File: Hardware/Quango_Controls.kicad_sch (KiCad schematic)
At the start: 36 parts, among them J1 Conn_01x12_Male, J10 Gate_Out, J2 Conn_01x16_Male, J3 Conn_01x14_Male, J4 Conn_01x12_Male, J5 CV_A, J6 CV_B, J7 Out, J8 USB_C_Receptacle, J9 Midi_In, SW1 SW_Push, SW2 SW_Push, SW3 Octave_Switch, U1 STF202-22T1G

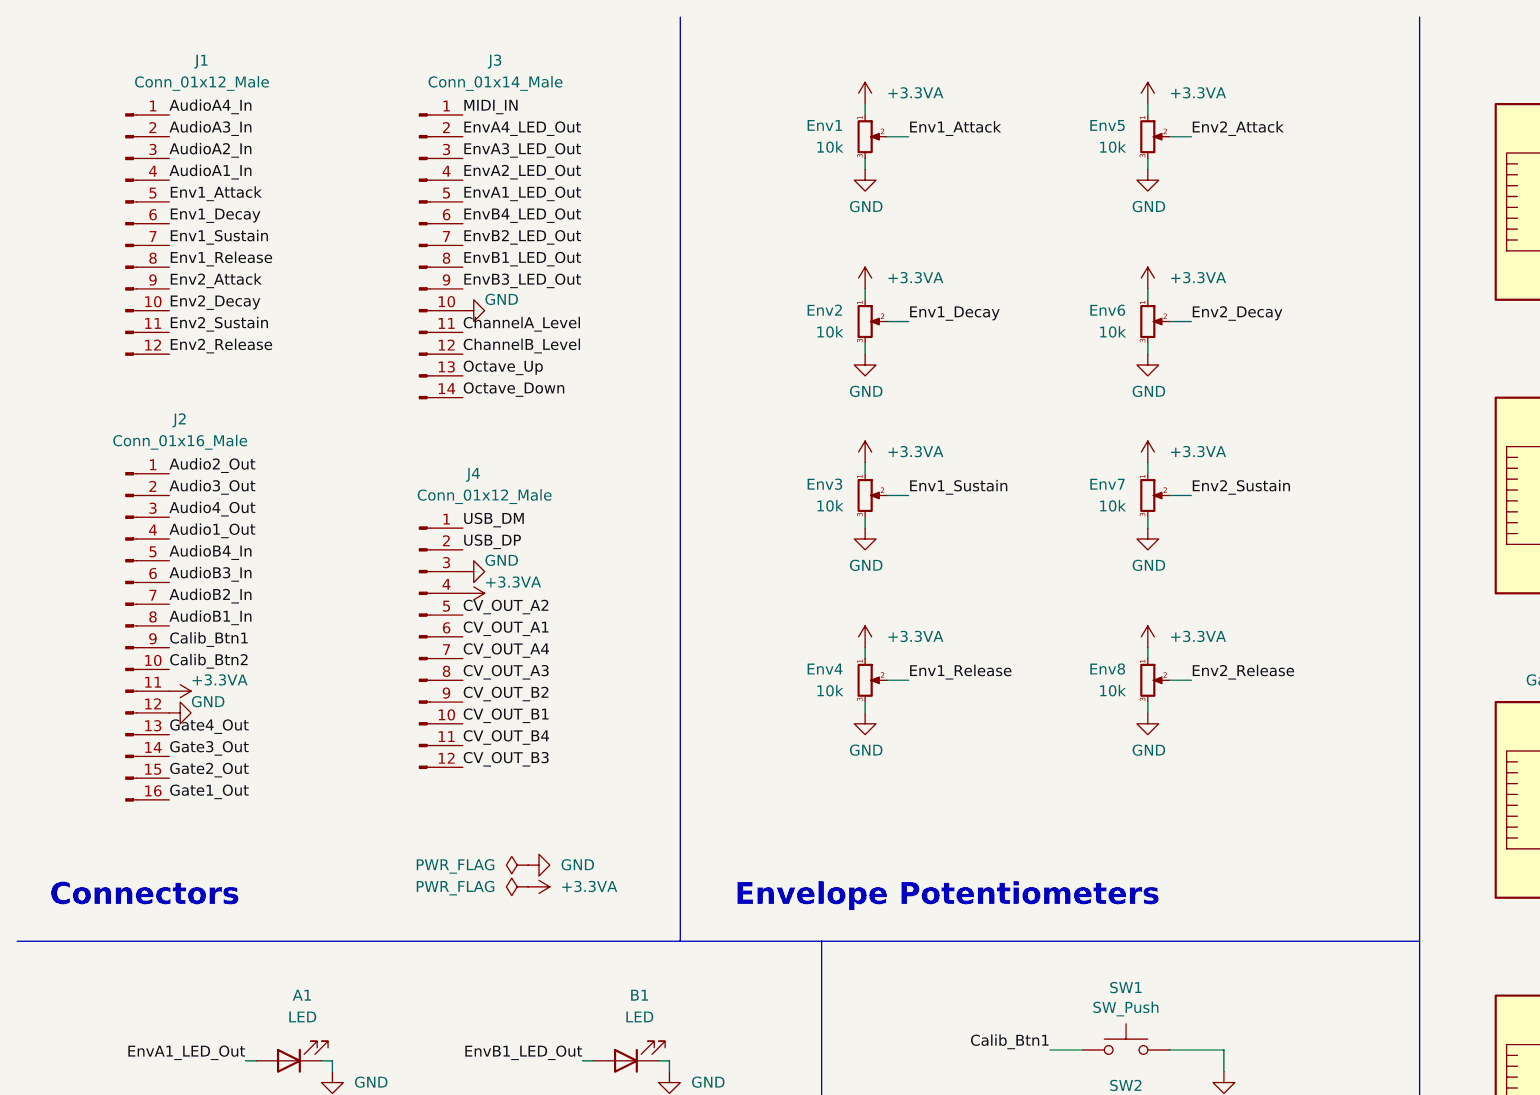
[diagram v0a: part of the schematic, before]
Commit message: Added header on control board for CV output
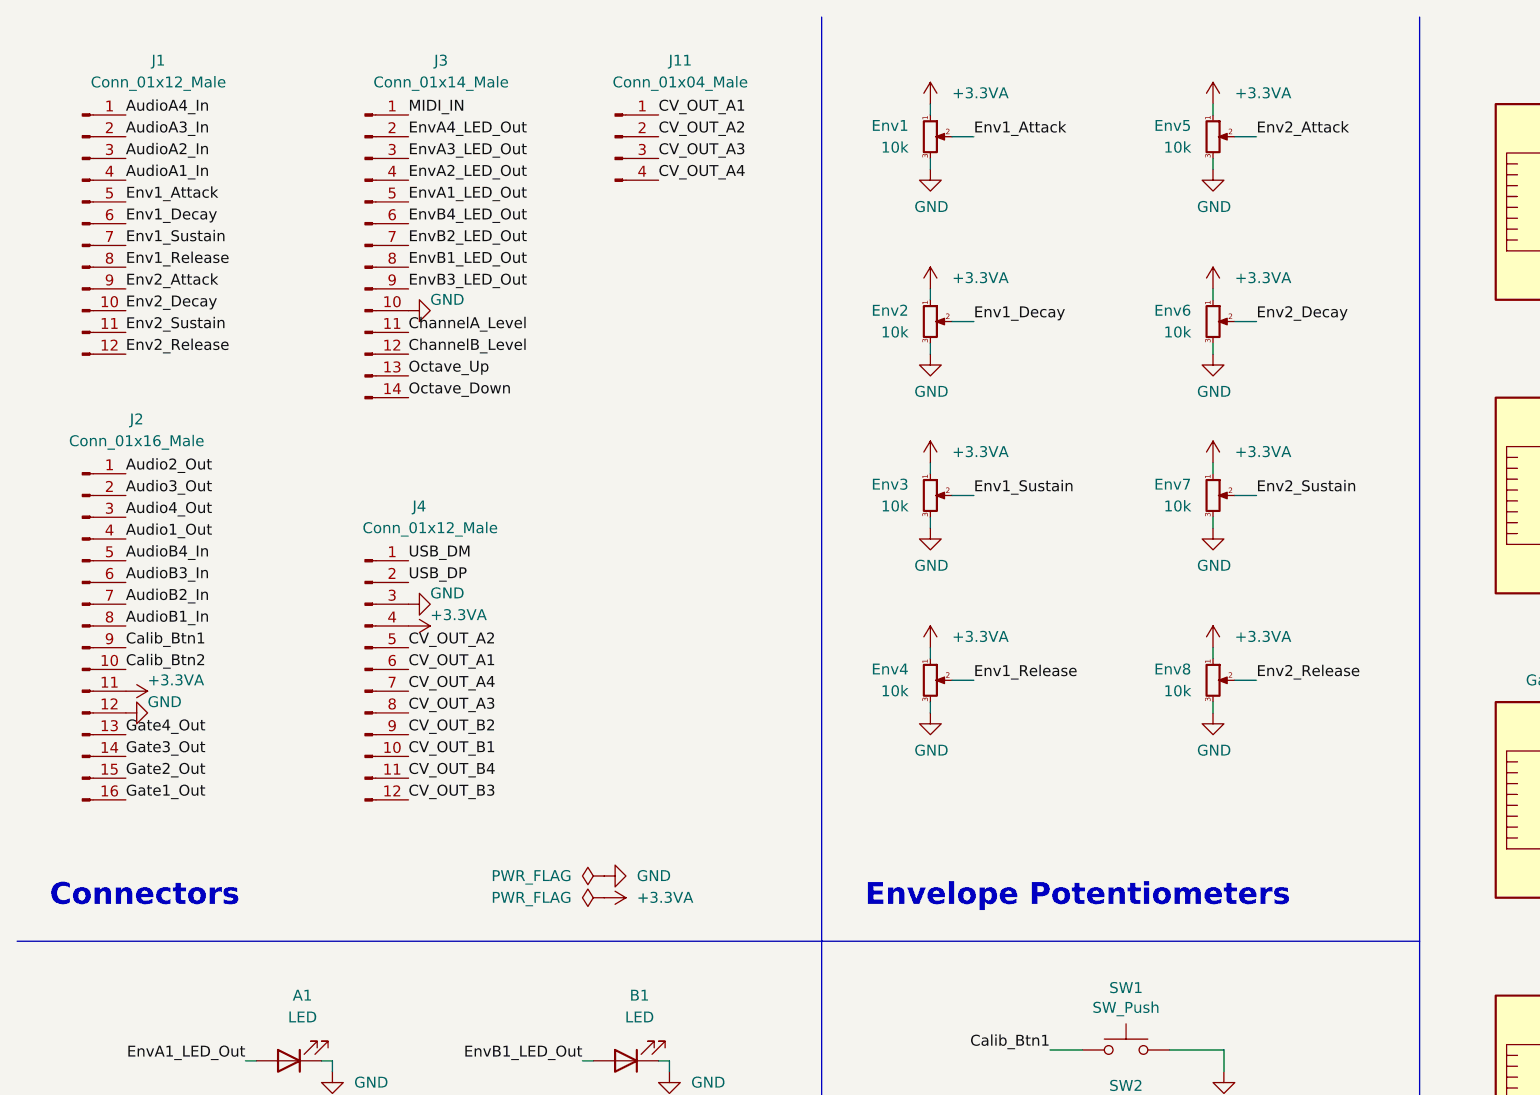
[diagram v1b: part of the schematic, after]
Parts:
- added J11: Conn_01x04_Male, Connector_PinHeader_2.54mm:PinHeader_1x04_P2.54mm_Vertical, symbol Connector:Conn_01x04_Male
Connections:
- net CV_OUT_A1: now also J11.1 (Pin_1)
- net CV_OUT_A2: now also J11.2 (Pin_2)
- net CV_OUT_A3: now also J11.3 (Pin_3)
- net CV_OUT_A4: now also J11.4 (Pin_4)
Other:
- moved on the sheet: Env1, Env2, Env3, Env4, Env5, Env6, Env7, Env8, J1, J2, J3, J4

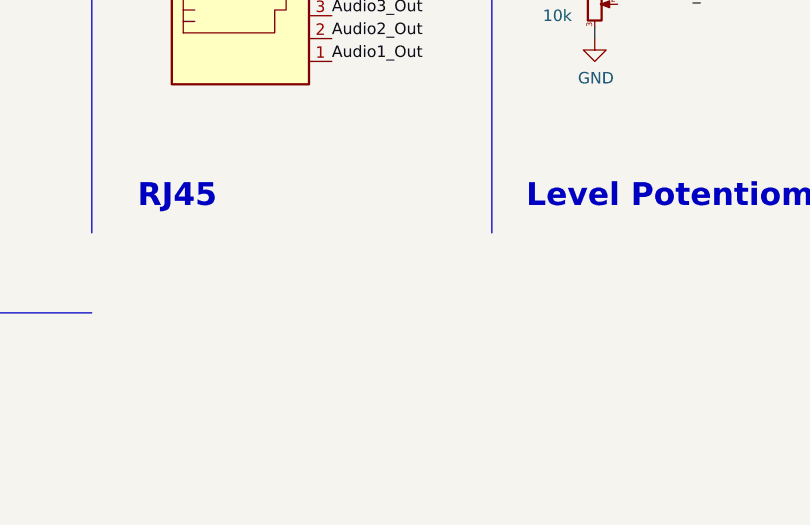
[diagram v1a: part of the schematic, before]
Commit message: Implemented octave up/down switch
Toggle CS on SPI2 to fix intermittent issue with external DAC
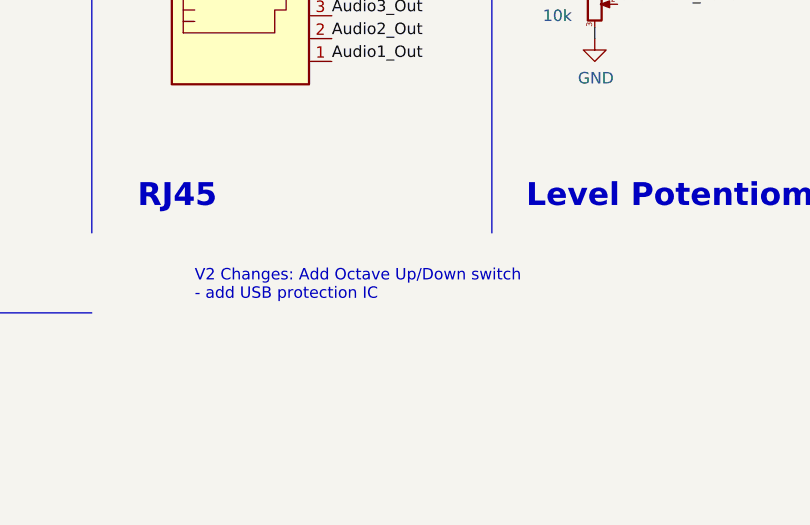
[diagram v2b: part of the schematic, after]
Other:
- note added: "V2 Changes: Add Octave Up/Down switch - add USB protection IC"
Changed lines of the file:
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@@
     (effects (font (size 2.54 2.54) (thickness 0.508) bold) (justify left bottom))
+  )
+  (text "V2 Changes: Add Octave Up/Down switch\n- add USB protection IC"
+    (at 187.96 173.99 0)
+    (effects (font (size 1.27 1.27)) (justify left bottom))
   )
   (label "CV_OUT_A3" (at 87.63 29.21 0)
